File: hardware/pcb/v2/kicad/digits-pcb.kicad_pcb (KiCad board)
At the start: 2 copper layers, 76.2 x 61.9 mm, 71 parts, among them J1 Conn_02x20_Odd_Even, J3 VIN_BARREL_PIGTAIL, J4 Conn_01x07, J6 Conn_01x02, J7 Screw_Terminal_01x02, J8 Conn_01x04, J9 Conn_01x03, SW1 SW_Push, U1 LM2596S-5, U2 DRV8871DDAR, U3 RP2040, U4 W25Q16JVSSIQ, U5 AMS1117-3.3, U6 TLV320AIC3104IRHBR, U7 XC6206P182MR, Y1 ABM8-272-T3

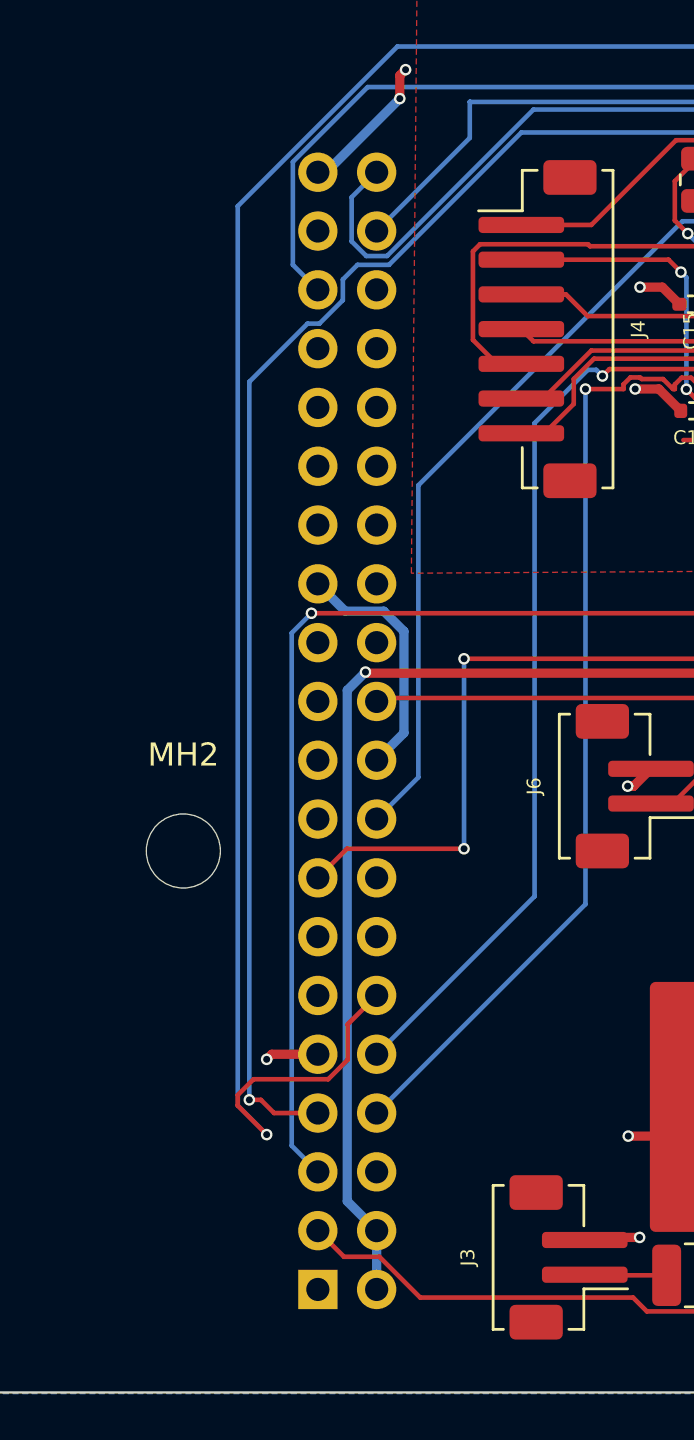
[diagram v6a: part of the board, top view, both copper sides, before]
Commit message: feat(hardware): verify LCSC parts, unify 100nF to 50V, move J1 to top
BOM verification pass on PCB v2:
- Fixed 3 wrong LCSC numbers (C5/C6 15pF, C10/C31 1uF, C12-C35/C56 100nF size)
- Filled 16 missing LCSC numbers across codec and ringer sub-sheets
- Unified all 100nF 0402 caps to C307331 (50V) since C54 is on +12V
- C55 updated to C336270 (47uF 25V Panasonic, D5xL5.8 — 2x derating for 12V rail)
- R5/R11 updated to in-stock C60490 (Yageo 10k 0402)
- COMPONENTS.md aligned with schematic

J1 body moved from B.Cu to F.Cu for Pi face-down mounting:
- Direct layer-string swap (B.Cu/SilkS/Fab/CrtYd -> F.*) without any
  coordinate mirror, so all 40 pin positions and routed traces stay
  intact. Removed stale (justify mirror) attributes from text fields.

DRC: 0 unconnected, 0 dangling, 0 clearance. Remaining 48 violations
are all cosmetic (silk + library drift).
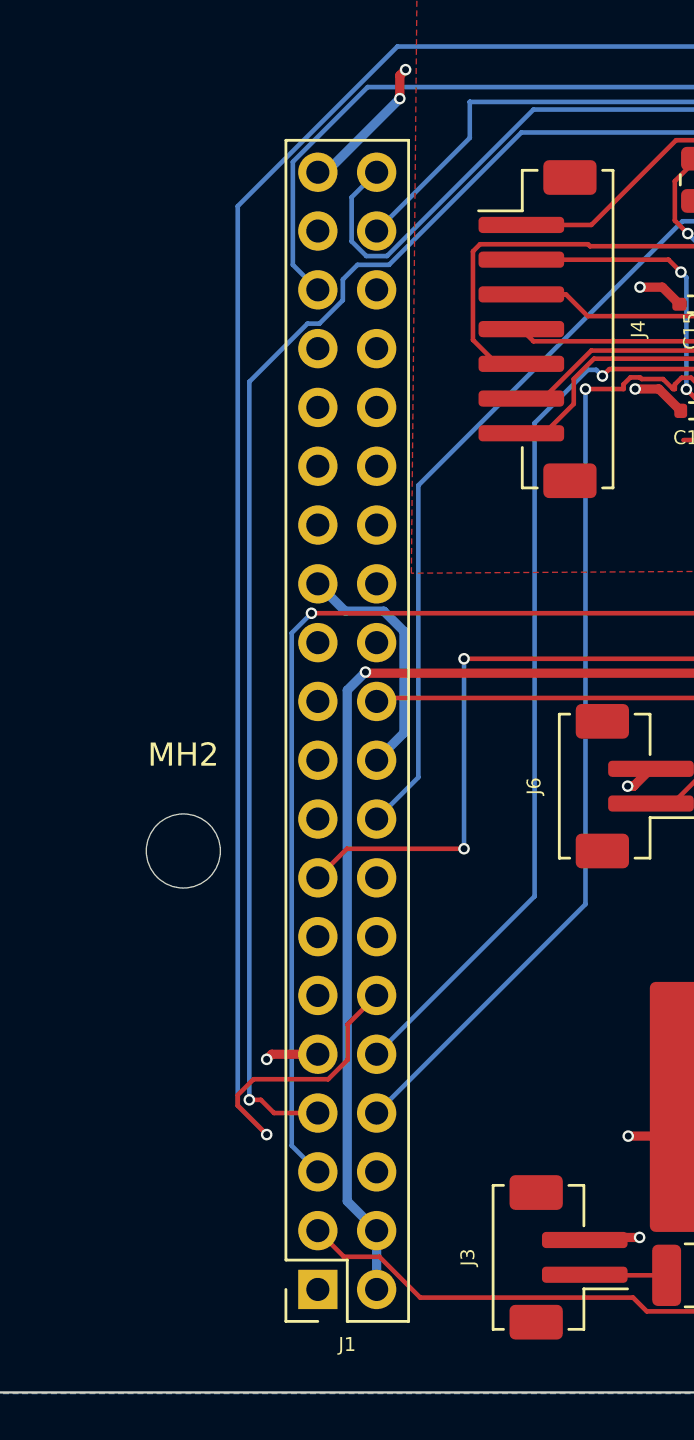
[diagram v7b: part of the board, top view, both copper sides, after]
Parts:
- J1: moved to F.Cu
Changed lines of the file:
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@@
 	)
 	(footprint "Connector_PinHeader_2.54mm:PinHeader_2x20_P2.54mm_Vertical"
-		(layer "B.Cu")
+		(layer "F.Cu")
 		(at 29.21 66.9)
 		(descr "Through hole straight pin header, 2x20, 2.54mm pitch, double rows")
@@
 		(property "Reference" "J1"
 			(at 1.27 2.38 0)
-			(layer "B.SilkS")
+			(layer "F.SilkS")
 			(effects
 				(font
@@
 					(thickness 0.1)
 				)
-				(justify mirror)
 			)
 		)
 		(property "Value" "Conn_02x20_Odd_Even"
 			(at 5.18 -38.91 0)
-			(layer "B.Fab")
-			(hide yes)
-			(effects
-				(font
-					(size 1 1)
-					(thickness 0.15)
-				)
-				(justify mirror)
+			(layer "F.Fab")
+			(hide yes)
+			(effects
+				(font
+					(size 1 1)
+					(thickness 0.15)
+				)
 			)
 		)
 		(property "Datasheet" ""
 			(at 0 0 0)
-			(layer "B.Fab")
+			(layer "F.Fab")
 			(hide yes)
 			(effects
@@
 					(size 1.27 1.27)
 				)
-				(justify mirror)
 			)
 		)
 		(property "Description" "Generic connector, double row, 02x20, odd/even pin numbering scheme (row 1 odd numbers, row 2 even numbers), script generated (kicad-library-utils/schlib/autogen/connector/)"
 			(at 0 0 0)
-			(layer "B.Fab")
+			(layer "F.Fab")
 			(hide yes)
 			(effects
@@
 					(size 1.27 1.27)
 				)
-				(justify mirror)
 			)
 		)
 		(property "KiLib_Generator" "connector/pin_header_socket"
 			(at 0 0 0)
-			(layer "B.SilkS")
-			(hide yes)
-			(effects
-				(font
-					(size 1 1)
-					(thickness 0.15)
-				)
-				(justify mirror)
+			(layer "F.SilkS")
+			(hide yes)
+			(effects
+				(font
+					(size 1 1)
+					(thickness 0.15)
+				)
 			)
 		)
@@
 			(at 0 0 0)
 			(unlocked yes)
-			(layer "B.Fab")
-			(hide yes)
-			(effects
-				(font
-					(size 1 1)
-					(thickness 0.15)
-				)
-				(justify mirror)
+			(layer "F.Fab")
+			(hide yes)
+			(effects
+				(font
+					(size 1 1)
+					(thickness 0.15)
+				)
 			)
 		)
@@
 				(type solid)
 			)
-			(layer "B.SilkS")
+			(layer "F.SilkS")
 		)
 		(fp_line
@@
 				(type solid)
 			)
-			(layer "B.SilkS")
+			(layer "F.SilkS")
 		)
 		(fp_line
@@
 				(type solid)
 			)
-			(layer "B.SilkS")
+			(layer "F.SilkS")
 		)
 		(fp_line
@@
 				(type solid)
 			)
-			(layer "B.SilkS")
+			(layer "F.SilkS")
 		)
 		(fp_line
@@
 				(type solid)
 			)
-			(layer "B.SilkS")
+			(layer "F.SilkS")
 		)
 		(fp_line
@@
 				(type solid)
 			)
-			(layer "B.SilkS")
+			(layer "F.SilkS")
 		)
 		(fp_line
@@
 				(type solid)
 			)
-			(layer "B.SilkS")
+			(layer "F.SilkS")
 		)
 		(fp_line
@@
 				(type solid)
 			)
-			(layer "B.SilkS")
+			(layer "F.SilkS")
 		)
 		(fp_rect
@@
 			)
 			(fill no)
-			(layer "B.CrtYd")
+			(layer "F.CrtYd")
 		)
 		(fp_line
@@
 				(type solid)
 			)
-			(layer "B.Fab")
+			(layer "F.Fab")
 		)
 		(fp_line
@@
 				(type solid)
 			)
-			(layer "B.Fab")
+			(layer "F.Fab")
 		)
 		(fp_line
@@
 				(type solid)
 			)
-			(layer "B.Fab")
+			(layer "F.Fab")
 		)
 		(fp_line
@@
 				(type solid)
 			)
-			(layer "B.Fab")
+			(layer "F.Fab")
 		)
 		(fp_line
@@
 				(type solid)
 			)
-			(layer "B.Fab")
+			(layer "F.Fab")
 		)
 		(fp_text user "${REFERENCE}"
 			(at 1.27 -24.13 90)
-			(layer "B.Fab")
-			(effects
-				(font
-					(size 1 1)
-					(thickness 0.15)
-				)
-				(justify mirror)
-			)
-		)
+			(layer "F.Fab")
+			(effects
+				(font
+					(size 1 1)
+					(thickness 0.15)
+				)
+			)
+		)

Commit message: fix(hardware): resolve 4 pre-fab blockers from final audit sweep
Six parallel audits identified three critical schematic blockers and
one safety concern. Each is resolved here without any PCB footprint
change (all parts share existing footprint pad patterns).

1. MIC_GND was floating — electret mic had no DC return. Renamed all
   MIC_GND labels (3 in schematic, 12 in PCB) to GND. The mic cold
   wire now grounds at J8.4 as codec-module-spec.md already described.
   One DRC airline remains between a segment of former-MIC-return
   copper and the main GND pour — user to add a single stitching via
   in pcbnew when reviewing.

2. J1 was assigned C50980 (BOOMELE 2x20 MALE pin header) which cannot
   mate with the Pi Zero 2 W's male GPIO header. Swapped to C2977589
   (ZHOURI 2.54-2x20 FEMALE socket, 17,970 in stock, same THT pad
   pattern, no PCB change).

3. Y1 was assigned C9002 (YXC 12MHz crystal with CL=20pF) while C5/C6
   are 15pF, sized for CL=10pF. Swapped to C20625731 (Abracon
   ABM8-272-T3, CL=10pF, datasheet-matched per RP2040 §2.16.1.1,
   13,480 in stock). Same 3225 4-pin SMD footprint.

4. F1 was assigned C70102 (TECHFUSE 1210 PTC, Vmax=6V) on the +12V
   rail, insufficient fault headroom. Swapped to C207048 (Littelfuse
   1210L150/16WR, Vmax=16V). Same 1210 footprint.

Also adds hardware/pcb/v2/SOFTWARE_CONFIG.md documenting Pi-side
dtoverlay, cmdline.txt, codec overlay, and OpenOCD requirements that
the carrier board assumes but cannot enforce. These are tracked as
a follow-up before bring-up, not blockers for fab.

Updated COMPONENTS.md and NET_TOPOLOGY.md to match. Production BOM
regenerated.
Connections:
- C3 pad 2: MIC_GND -> GND
- J8 pad 4: MIC_GND -> GND
- J9 pad 3: MIC_GND -> GND
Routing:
- net MIC_GND: track 21.2 -> 0.00 mm
- net GND: track 218.8 -> 240.0 mm
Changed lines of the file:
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@@
 			(layers "F.Cu" "F.Mask" "F.Paste")
 			(roundrect_rratio 0.25)
-			(net "MIC_GND")
+			(net "GND")
 			(pintype "passive")
 		)
@@
 			(layers "F.Cu" "F.Mask" "F.Paste")
 			(roundrect_rratio 0.25)
-			(net "MIC_GND")
+			(net "GND")
 			(pinfunction "Pin_4_4")
 			(pintype "passive")
@@
 			(layers "F.Cu" "F.Mask" "F.Paste")
 			(roundrect_rratio 0.25)
-			(net "MIC_GND")
+			(net "GND")
 			(pinfunction "Pin_3_3")
 			(pintype "passive")
@@
 		(width 0.2)
 		(layer "F.Cu")
-		(net "MIC_GND")
+		(net "GND")
 	)
 	(segment
@@
 		(width 0.2)
 		(layer "F.Cu")
-		(net "MIC_GND")
+		(net "GND")
 	)
 	(segment
@@
 		(width 0.2)
 		(layer "F.Cu")
-		(net "MIC_GND")
+		(net "GND")
 	)
 	(segment
@@
 		(width 0.2)
 		(layer "F.Cu")
-		(net "MIC_GND")
+		(net "GND")
 	)
 	(segment
@@
 		(width 0.2)
 		(layer "F.Cu")
-		(net "MIC_GND")
+		(net "GND")
 	)
 	(segment
@@
 		(width 0.2)
 		(layer "F.Cu")
-		(net "MIC_GND")
+		(net "GND")
 	)
 	(segment
@@
 		(width 0.2)
 		(layer "F.Cu")
-		(net "MIC_GND")
+		(net "GND")
 	)
 	(segment
@@
 		(width 0.2)
 		(layer "F.Cu")
-		(net "MIC_GND")
+		(net "GND")
 	)
 	(segment
@@
 		(width 0.2)
 		(layer "F.Cu")
-		(net "MIC_GND")
+		(net "GND")
 	)
 	(segment
